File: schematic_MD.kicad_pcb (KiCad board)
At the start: 2 copper layers, 100 x 100 mm, 153 parts, among them J1 XT60, J10 Gate_PWR_Jump, J11 CAN_Bus, J13 EXPWR_GND, J2 XT60, J3 XT60, J4 CAN_Bus, J5 Rotaly_encoder_1, J6 Rotaly_encoder_2, J7 Conn_02x07_Odd_Even, J9 Conn_02x01, Q1 SQJ886EP-T1_GE3, Q2 SQJ886EP-T1_GE3, Q3 SQJ886EP-T1_GE3, Q4 SQJ886EP-T1_GE3, Q5 SQJ886EP-T1_GE3, Q6 SQJ886EP-T1_GE3, Q7 SQJ886EP-T1_GE3, Q8 SQJ886EP-T1_GE3, SW1 SW_MEC_5G, U1 UCC21520DW, U11 74HC04, U2 XC6206P332MR-G, U3 UCC21520DW, U4 UCC21520DW, U5 UCC21520DW, U6 STM32F405RGTx, U7 MAX3051, U8 L78M05ABDT-TR, Y1 25MHz, Y2 Crystal

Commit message: precompleate PCB design
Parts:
- removed C43: 1uF, Capacitor_SMD:C_0603_1608Metric_Pad1.08x0.95mm_HandSolder
- added H1: MountingHole_Pad, MountingHole:MountingHole_3.2mm_M3_Pad_Via, F.Cu at (98.5, 43.5)
- added H2: MountingHole_Pad, MountingHole:MountingHole_3.2mm_M3_Pad_Via, F.Cu at (98.5, 136.5)
- added H3: MountingHole_Pad, MountingHole:MountingHole_3.2mm_M3_Pad_Via, F.Cu at (191.5, 43.5)
- added H4: MountingHole_Pad, MountingHole:MountingHole_3.2mm_M3_Pad_Via, F.Cu at (191.5, 136.5)
- moved J6 85.7 mm to (108.5, 129.1), turned to 180 degrees
- moved J5 78.7 mm to (108.5, 121.6), turned to 180 degrees
- moved R18 25.7 mm to (121.8, 43.7), turned to 180 degrees
- moved D8 24.2 mm to (118.3, 43.8), turned to 0 degrees
- moved R17 23.4 mm to (121.8, 45.4), turned to 180 degrees
- moved D7 21.8 mm to (118.3, 45.5), turned to 0 degrees
- moved R16 21.1 mm to (121.8, 47.2), turned to 180 degrees
- moved D6 19.5 mm to (118.3, 47.2), turned to 0 degrees
- moved C30 19.4 mm to (107.8, 90.7), turned to 90 degrees
- moved D5 17.1 mm to (107.5, 53.1)
- moved C28 16.9 mm to (99.7, 108.8)
- moved C31 16.9 mm to (110.0, 111.4)
- moved C32 16.9 mm to (103.0, 112.0)
- moved C33 16.9 mm to (98.2, 107.0)
- moved C37 16.9 mm to (113.2, 105.5)
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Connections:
- C47 pad 1: /Driver/EN_right -> /Driver/EN_left
- C48 pad 1: /Driver1/EN_right -> /Driver1/EN_left
- J5 pad 3: unconnected-(J5-Pin_3-Pad3) -> /STM32F405/Motor1_A
- J5 pad 4: unconnected-(J5-Pin_4-Pad4) -> /STM32F405/Motor1_B
- J5 pad 5: unconnected-(J5-Pin_5-Pad5) -> /STM32F405/Motor1_Z
- J6 pad 3: unconnected-(J6-Pin_3-Pad3) -> /STM32F405/Motor2_A
- J6 pad 4: unconnected-(J6-Pin_4-Pad4) -> /STM32F405/Motor2_B
- J6 pad 5: unconnected-(J6-Pin_5-Pad5) -> /STM32F405/Motor2_Z
- R22 pad 2: /Driver/EN_right -> /Driver/EN_left
- R23 pad 2: /Driver1/EN_right -> /Driver1/EN_left
- U4 pad 5: /Driver/EN_right -> /Driver/EN_left
- U5 pad 5: /Driver1/EN_right -> /Driver1/EN_left
- U6 pad 15: unconnected-(U6-PA1-Pad15) -> /STM32F405/Motor1_Z
- U6 pad 16: unconnected-(U6-PA2-Pad16) -> /STM32F405/Motor1_B
- U6 pad 17: unconnected-(U6-PA3-Pad17) -> /STM32F405/Motor1_A
- U6 pad 23: unconnected-(U6-PA7-Pad23) -> /STM32F405/Motor2_Z
- U6 pad 26: unconnected-(U6-PB0-Pad26) -> /STM32F405/Motor2_B
- U6 pad 27: unconnected-(U6-PB1-Pad27) -> /STM32F405/Motor2_A
- U6 pad 33: unconnected-(U6-PB12-Pad33) -> /Driver/EN_left
- U6 pad 37: unconnected-(U6-PC6-Pad37) -> /Driver/Left_Highside_PWM_IN
- U6 pad 38: unconnected-(U6-PC7-Pad38) -> /Driver/Right_Highside_PWM_IN
- U6 pad 39: unconnected-(U6-PC8-Pad39) -> /Driver1/Left_Highside_PWM_IN
- U6 pad 40: unconnected-(U6-PC9-Pad40) -> /Driver1/Right_Highside_PWM_IN
- U6 pad 41: unconnected-(U6-PA8-Pad41) -> /Driver1/EN_left
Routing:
- net +5V: track 73.7 -> 164.5 mm, vias 0 -> 2
- net /Driver/EN_left: track 4.83 -> 60.0 mm, vias 0 -> 6
- net /Driver1/Right_Highside_PWM_IN: track 0.00 -> 49.4 mm, vias 0 -> 2
- net /Driver1/EN_left: track 4.75 -> 49.5 mm, vias 0 -> 5
- net /Driver/Left_Highside_PWM_IN: track 0.00 -> 44.1 mm, vias 0 -> 4
- net /STM32F405/NRST: track 21.6 -> 64.9 mm, vias 2 -> 8
- net /STM32F405/Motor2_A: track 0.00 -> 39.3 mm, vias 0 -> 2
- net /STM32F405/Motor2_B: track 0.00 -> 38.7 mm, vias 0 -> 2
- net /STM32F405/Motor2_Z: track 0.00 -> 38.5 mm, vias 0 -> 2
- net /Driver1/Right_Lowside_PWM_IN: track 0.00 -> 34.6 mm
- net /Driver1/Left_Highside_PWM_IN: track 0.00 -> 32.8 mm, vias 0 -> 4
- net /Driver/Right_Highside_PWM_IN: track 0.00 -> 32.1 mm, vias 0 -> 4
- net /Driver/Left_Lowside_PWM_IN: track 0.00 -> 26.8 mm
- net /STM32F405/Motor1_Z: track 0.00 -> 22.7 mm, vias 0 -> 2
- net /STM32F405/Motor1_A: track 0.00 -> 22.4 mm, vias 0 -> 2
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- added copper zone on F.Cu, net GND1
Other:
- outline, holes or cut-outs redrawn
- board text added: "終端抵抗"

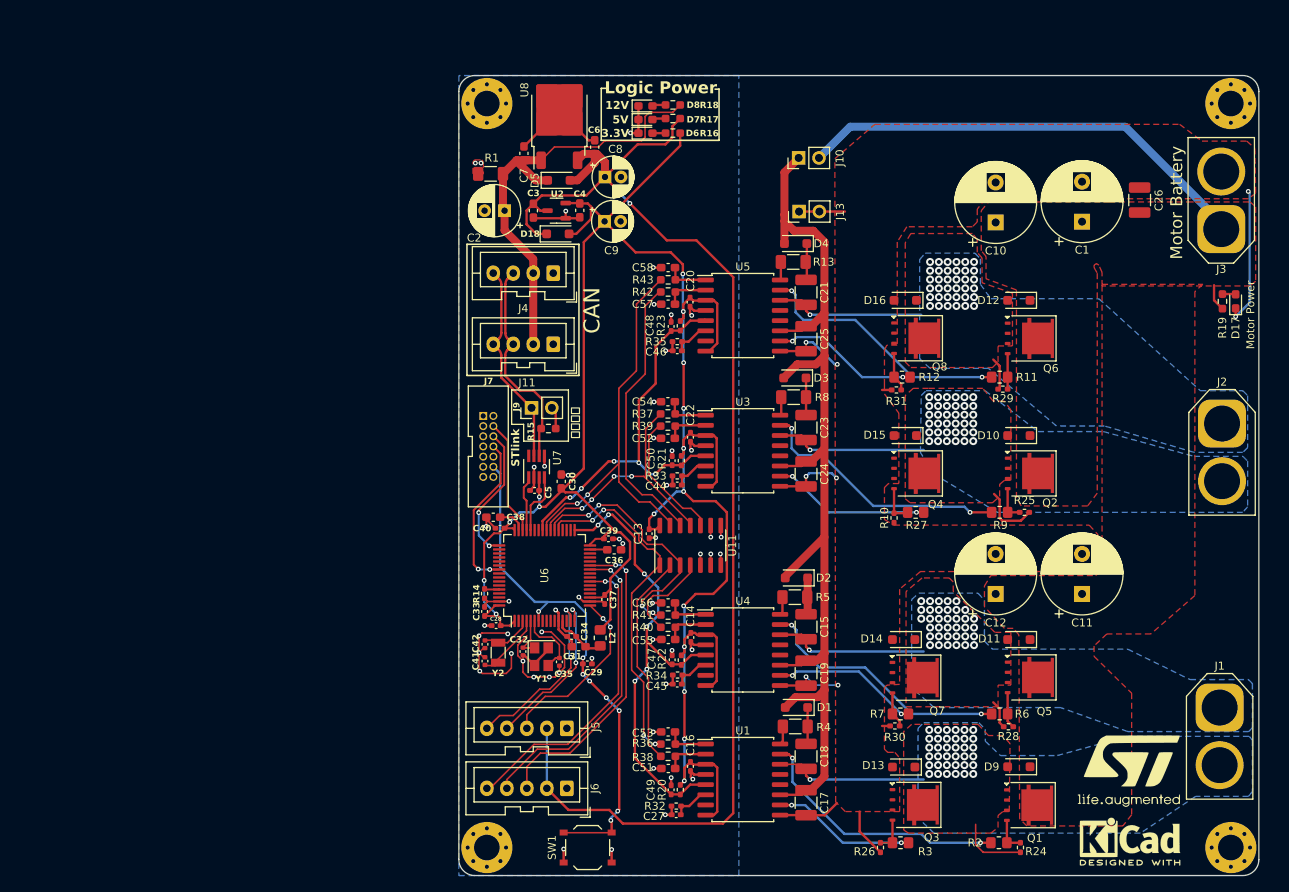
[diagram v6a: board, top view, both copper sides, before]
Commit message: add gatedriver power
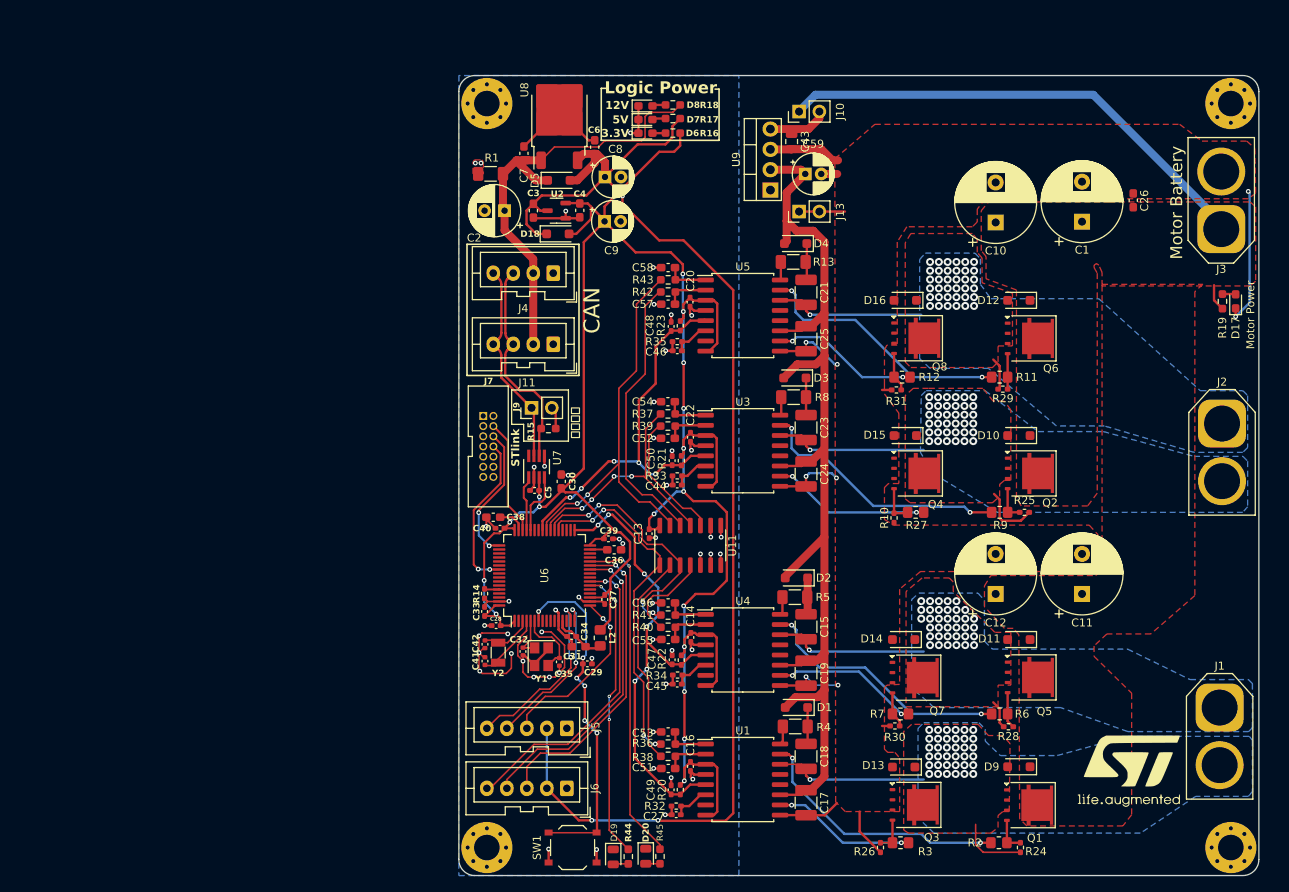
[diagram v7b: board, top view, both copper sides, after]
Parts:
- removed REF**: KiCad-Logo2_5mm_SilkScreen, Symbol:KiCad-Logo2_5mm_SilkScreen
- added C43: 0.47uF, Capacitor_SMD:C_0805_2012Metric, F.Cu at (136.6, 48.2)
- added C59: 22uF, Capacitor_THT:CP_Radial_D5.0mm_P2.00mm, F.Cu at (138.3, 52.3)
- added D19: LED, LED_SMD:LED_0805_2012Metric, F.Cu at (114.3, 137.7)
- added D20: LED, LED_SMD:LED_0805_2012Metric, F.Cu at (118.4, 137.6)
- added R44: 330, Resistor_SMD:R_0603_1608Metric_Pad0.98x0.95mm_HandSolder, F.Cu at (116.2, 137.6)
- added R45: 330, Resistor_SMD:R_0603_1608Metric_Pad0.98x0.95mm_HandSolder, F.Cu at (120.1, 137.6)
- added U9: NJM2396F12, Package_TO_SOT_THT:TO-220-4_Vertical, F.Cu at (133.9, 54.3)
- C26: value 10u -> 1uF; footprint Capacitor_SMD:C_1210_3225Metric_Pad1.33x2.70mm_HandSolder -> Capacitor_SMD:C_0603_1608Metric_Pad1.08x0.95mm_HandSolder
- moved J10 5.80 mm to (137.5, 44.5)
- moved SW1 1.88 mm to (109.2, 136.5)
- moved C26 0.80 mm to (179.3, 55.6)
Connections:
- J10 pad 1: Gate_power -> Vdrive
- J10 pad 2: Vdrive -> Net-(J10-Pin_2)
- U6 pad 22: unconnected-(U6-PA6-Pad22) -> Net-(U6-PA6)
- U6 pad 28: unconnected-(U6-PB2-Pad28) -> Net-(U6-PB2)
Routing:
- net Net-(U6-PB2): track 0.00 -> 42.3 mm, vias 0 -> 2
- net Net-(U6-PA6): track 0.00 -> 36.5 mm, vias 0 -> 4
- net /STM32F405/NRST: track 64.9 -> 43.3 mm, vias 8 -> 6
- net GND2: track 66.1 -> 77.1 mm
- net Net-(J10-Pin_2): track 0.00 -> 7.52 mm
- net Vdrive: track 60.5 -> 64.0 mm
- net Gate_power: track 128.8 -> 131.4 mm
- net Net-(D19-A): track 0.00 -> 1.91 mm
- net Net-(D20-A): track 0.00 -> 1.78 mm
- net +3.3V: track 276.5 -> 277.6 mm
- net +5V: track 164.5 -> 163.8 mm, vias 2 -> 4
